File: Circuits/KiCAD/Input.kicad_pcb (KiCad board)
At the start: 2 copper layers, 0 parts

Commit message: KiCAD,EAGLEでのPCB設計を試行中。
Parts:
- added 0.22F1: C, C1V5, F.Cu at (59.7, 52.1)
- added 2M1: R, R3, F.Cu at (85.1, 50.8)
- added BT1: BATTERY, CR2032H, F.Cu at (41.9, 50.8)
- added CFG1: CONN_2, PIN_ARRAY_2X1, F.Cu at (85.1, 44.5)
- added REED1: SPST, PIN_ARRAY_2X1, F.Cu at (90.2, 44.5)
- added U1: LITE_LITE, TQFP32, F.Cu at (73.7, 48.3)
- added WRITER1: CONN_5, PIN_ARRAY_5x1, F.Cu at (59.7, 43.2)

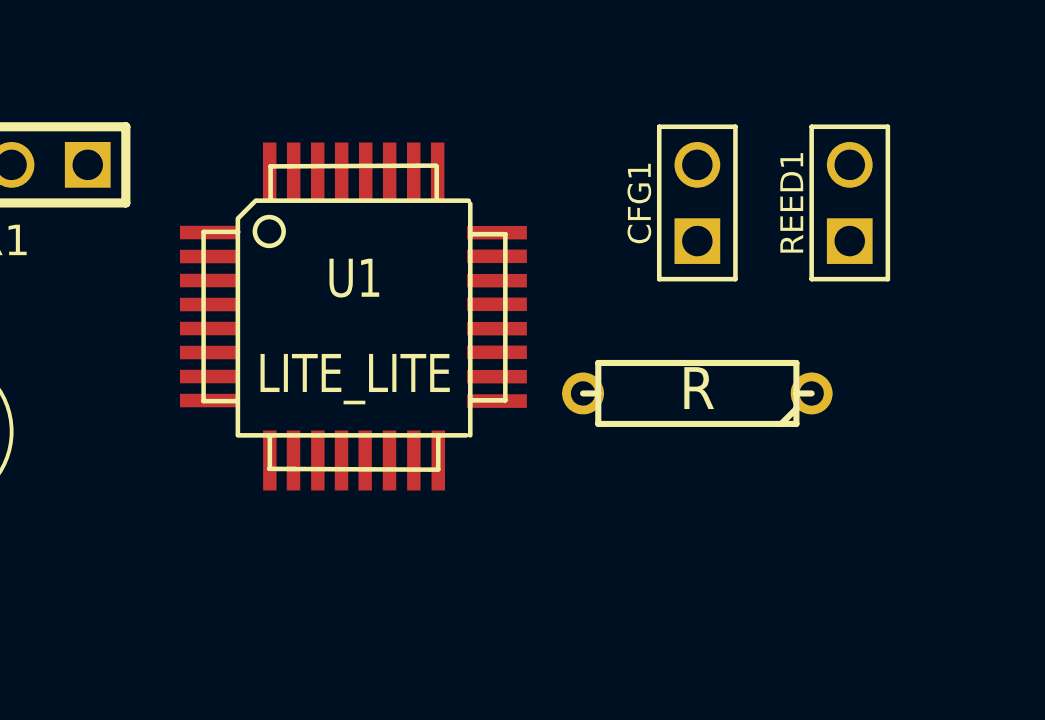
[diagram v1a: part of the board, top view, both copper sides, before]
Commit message: TWE-Lite SMDのパッド位置修正、外形線追加。
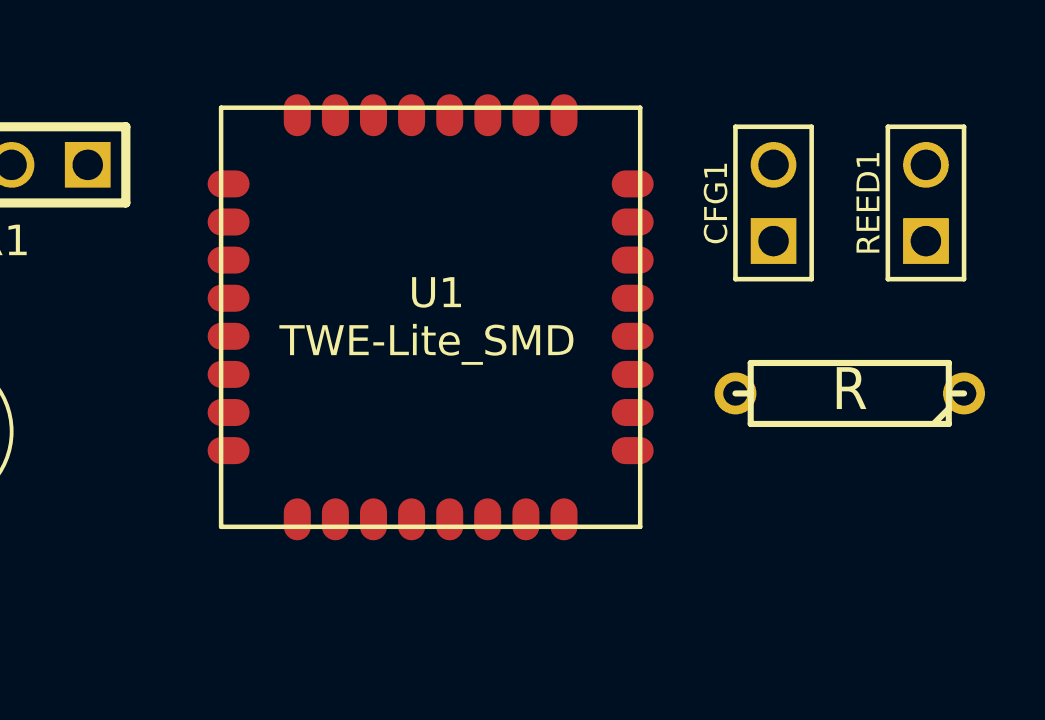
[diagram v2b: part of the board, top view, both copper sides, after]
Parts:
- U1: value LITE_LITE -> TWE-Lite_SMD; footprint TQFP32 -> TWE-Lite_SMD
- moved 2M1 5.08 mm to (90.2, 50.8)
- moved U1 2.54 mm to (76.2, 48.3)
- moved CFG1 2.54 mm to (87.6, 44.5)
- moved REED1 2.54 mm to (92.7, 44.5)

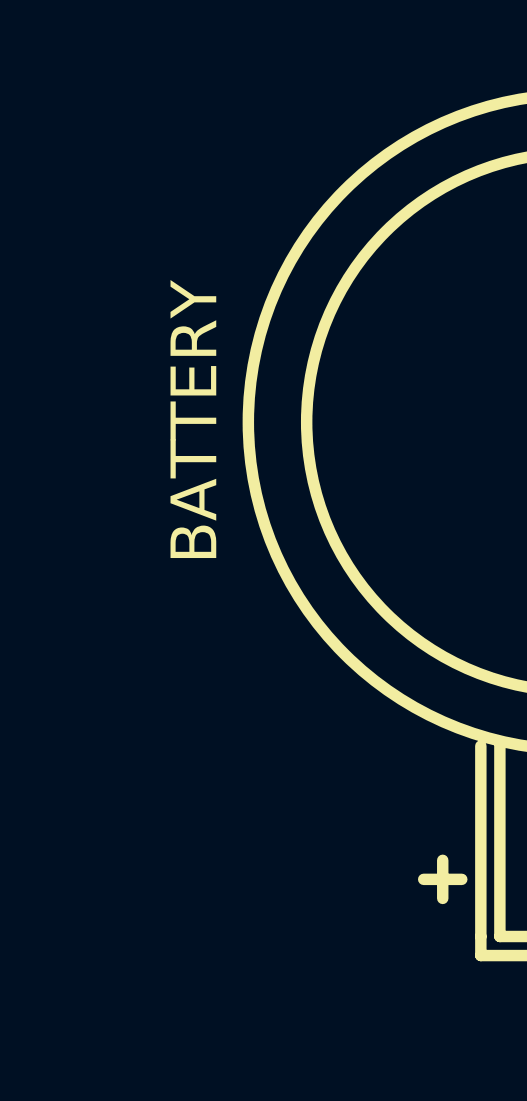
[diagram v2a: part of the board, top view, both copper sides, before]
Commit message: TWE-EH Solar版回路図を差し替え。
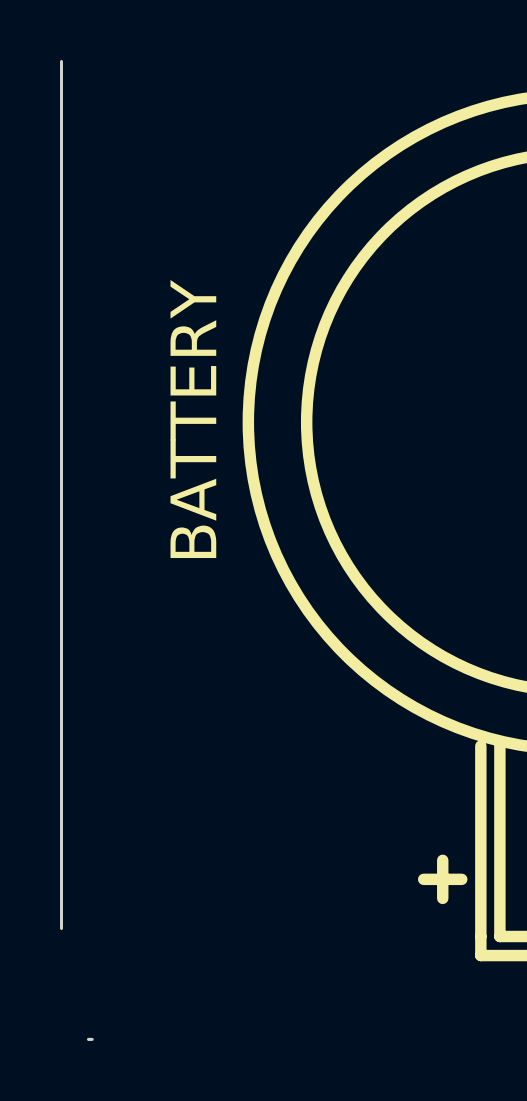
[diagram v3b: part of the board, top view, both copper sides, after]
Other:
- board outline added: 1 x 32.6 mm
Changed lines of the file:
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@@
     (area 28.0416 39.430546 94.9325 69.024501)
     (thickness 1.6)
-    (drawings 0)
+    (drawings 2)
     (tracks 0)
     (zones 0)
@@
     )
   )
+  (gr_line (start 25.781 71.374) (end 25.654 71.374) (angle 90) (layer Edge.Cuts) (width 0.1))
+  (gr_line (start 24.757 38.778) (end 24.757 67.678) (angle 90) (layer Edge.Cuts) (width 0.1))
 )

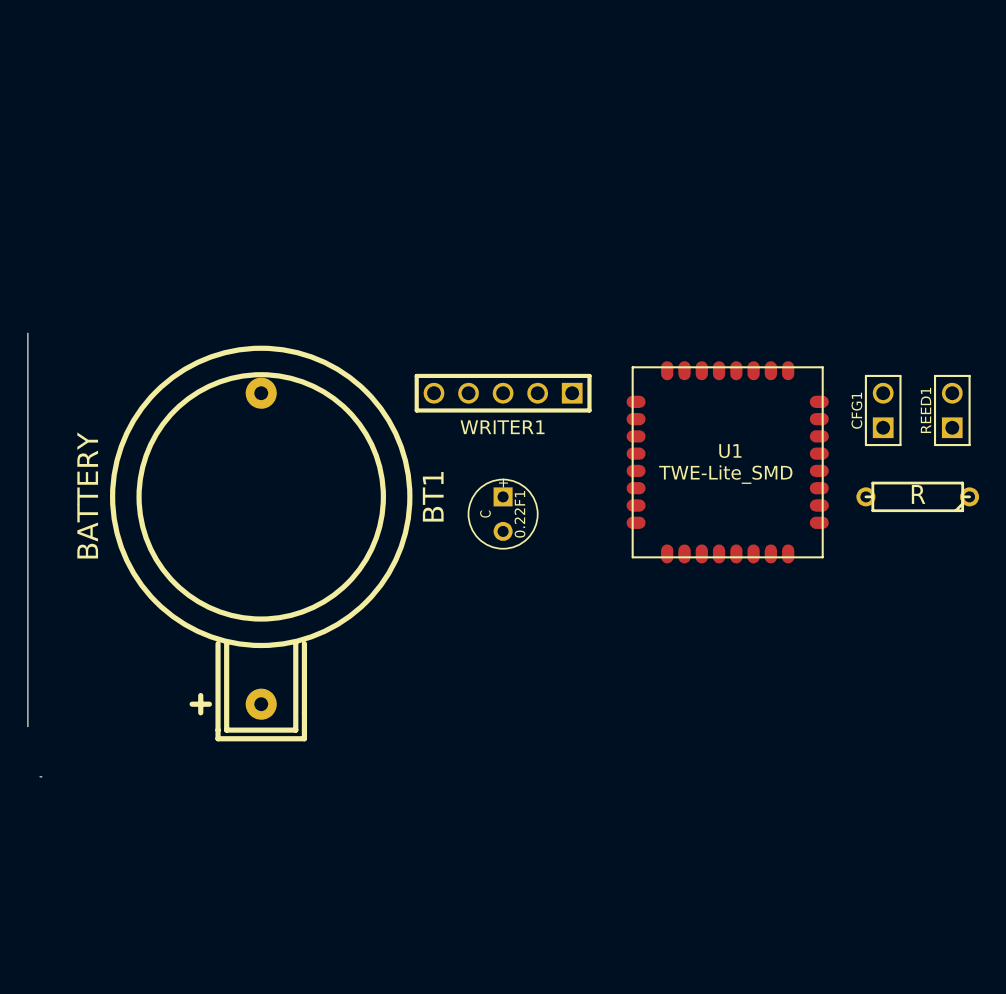
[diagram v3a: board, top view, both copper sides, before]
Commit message: Assigned PBCS-75 as battery holder.
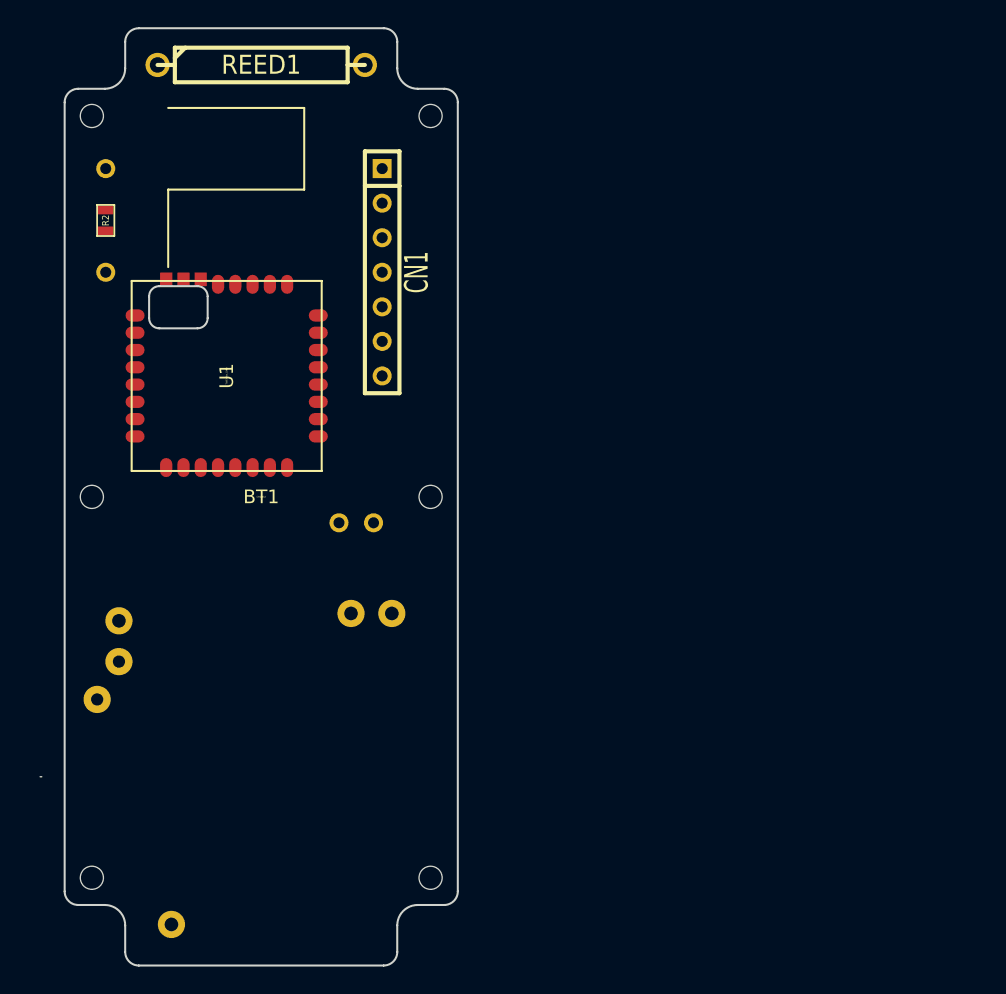
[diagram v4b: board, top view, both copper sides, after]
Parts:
- removed 0.22F1: C, C1V5
- removed 2M1: R, R3
- removed CFG1: CONN_2, PIN_ARRAY_2X1
- removed WRITER1: CONN_5, PIN_ARRAY_5x1
- added C1: 0.22, C1, B.Cu at (48.9, 52.7)
- added CN1: WRITER, SIL-7, F.Cu at (50.8, 34.3)
- added R1: 2M, R3, B.Cu at (30.5, 30.5)
- added R2: 2M, SM0603, F.Cu at (30.5, 30.5)
- BT1: value BATTERY -> CR2032; footprint CR2032H -> PBCS-75
- REED1: footprint PIN_ARRAY_2X1 -> R6
- U1: footprint TWE-Lite_SMD -> TWE-001L-SMD
- moved REED1 56.8 mm to (41.9, 19.1), turned to 0 degrees
- moved U1 37.4 mm to (39.4, 41.9), turned to 270 degrees
- turned BT1 to 0 degrees
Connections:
- net N-0000027 renamed /DOOR
- REED1 pad 1: N-0000032 -> /PULLUP
- U1 pad 2: N-0000030 -> /PRG
- U1 pad 21: N-0000029 -> /RST
- U1 pad 27: N-0000023 -> /CFG
- U1 pad 8: N-0000031 -> /TX
- U1 pad 9: N-0000014 -> /RX
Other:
- board size 1 x 32.6 mm -> 28.9 x 68.9 mm

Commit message: Added small EDLC module.
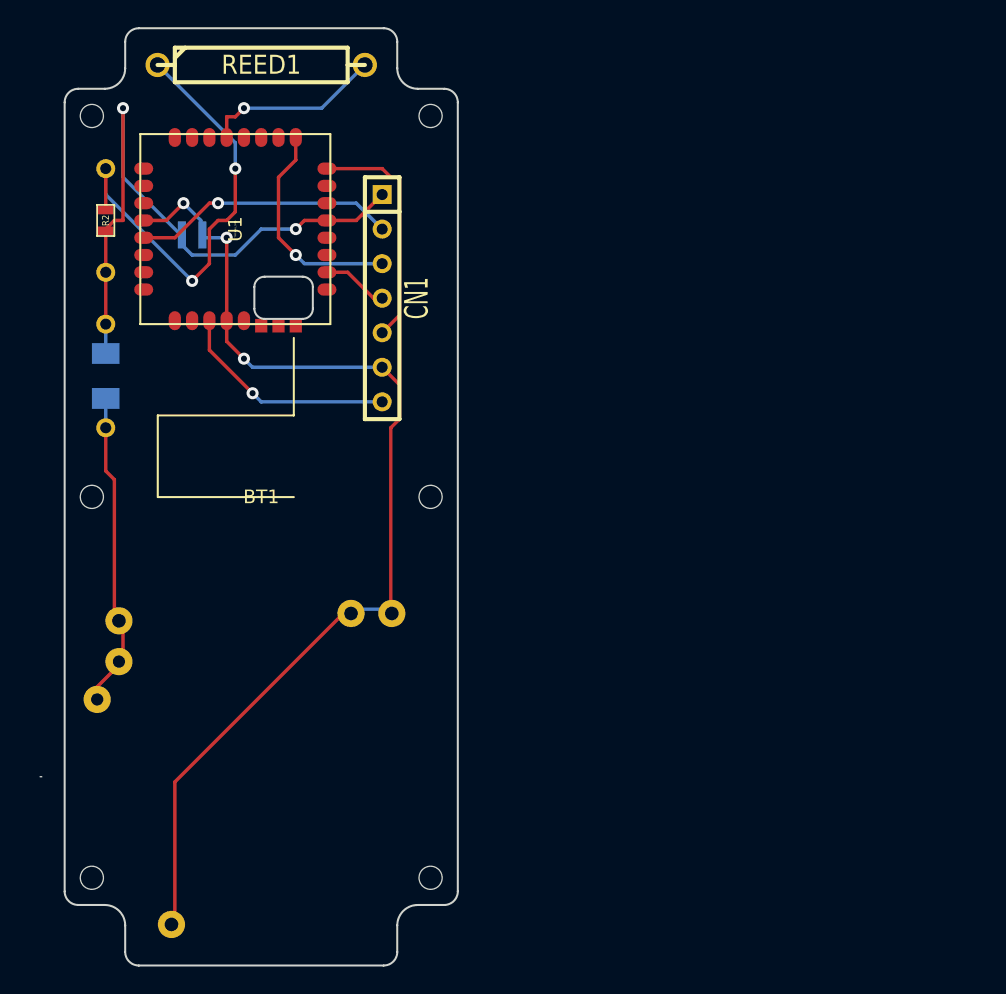
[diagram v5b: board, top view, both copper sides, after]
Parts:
- added R3: 75, R3, B.Cu at (30.5, 41.9)
- added R4: 75, SM1206, B.Cu at (30.5, 41.9)
- C1: footprint C1 -> DCK-3R3E224-E
- moved C1 20.4 mm to (36.8, 36.2), turned to 0 degrees
- moved U1 10.8 mm to (40.0, 31.1), turned to 90 degrees
- moved CN1 1.91 mm to (50.8, 36.2)
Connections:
- BT1 pad 1: VCC -> /DC3V
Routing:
- net GND: track 0.00 -> 80.4 mm, vias 0 -> 3
- net VCC: track 0.00 -> 48.1 mm, vias 0 -> 2
- net /PULLUP: track 0.00 -> 33.9 mm, vias 0 -> 2
- net /DC3V: track 0.00 -> 24.8 mm
- net /RST: track 0.00 -> 19.4 mm, vias 0 -> 1
- net /TX: track 0.00 -> 17.5 mm
- net /CFG: track 0.00 -> 16.4 mm, vias 0 -> 1
- net /RX: track 0.00 -> 16.3 mm, vias 0 -> 1
- net /DOOR: track 0.00 -> 13.3 mm, vias 0 -> 1
- net /PRG: track 0.00 -> 4.85 mm

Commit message: Use chip registers.
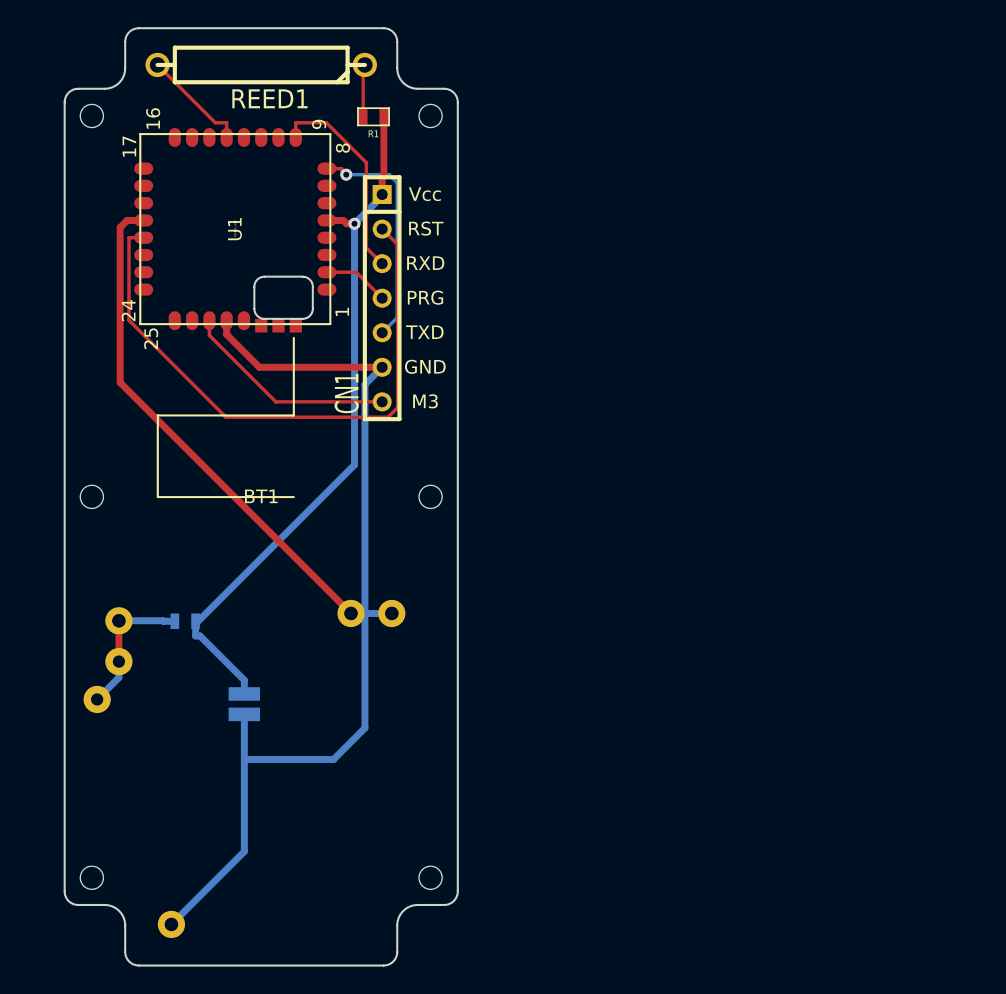
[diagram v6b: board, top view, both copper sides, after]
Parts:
- removed R3: 75, R3
- removed R4: 75, SM1206
- R1: footprint R3 -> SM0603; moved to F.Cu
- R2: value 2M -> 75; moved to B.Cu
- moved C1 31.1 mm to (45.7, 66.0), turned to 90 degrees
- moved R2 30.0 mm to (36.3, 59.9), turned to 0 degrees
- moved R1 21.1 mm to (50.2, 22.9), turned to 0 degrees
- turned REED1 to 180 degrees
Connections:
- C1 pad 1: GND -> VCC
- C1 pad 2: VCC -> GND
- R2 pad 1: VCC -> /DC3V
- R2 pad 2: /PULLUP -> VCC
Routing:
- net /PULLUP: track 33.9 -> 3.86 mm, vias 2 -> 0
- net GND: track 80.4 -> 108.3 mm, vias 3 -> 0
- net /RST: track 19.4 -> 43.7 mm, vias 1 -> 0
- net /DC3V: track 24.8 -> 10.6 mm
- net /DOOR: track 13.3 -> 7.92 mm, vias 1 -> 0
- net VCC: track 48.1 -> 52.3 mm, vias 2 -> 1
- net /RX: track 16.3 -> 15.4 mm, vias 1 -> 0
- net /CFG: track 16.4 -> 15.8 mm, vias 1 -> 0
- net /TX: track 17.5 -> 17.1 mm, vias 0 -> 1
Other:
- net class power added: clearance 0.254, trace_width 0.508, via_dia 0.889, via_drill 0.635
- board text added: "GND"
- board text added: "M3"
- board text added: "PRG"
- board text added: "RST"
- board text added: "RXD"
- board text added: "TXD"
- board text added: "Vcc"
